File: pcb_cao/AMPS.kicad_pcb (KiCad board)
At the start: 2 copper layers, 80 x 36.2 mm, 21 parts, among them J1 Conn_01x02, J10 Conn_01x02, J11 Conn_01x02, J12 Conn_01x16, J2 Conn_01x02, J3 Conn_01x02, J4 Conn_01x02, J5 Conn_01x03, J6 Conn_01x03, J7 Conn_01x03, J8 Conn_01x03, U1 ARDUINO_MICRO_SHIELD

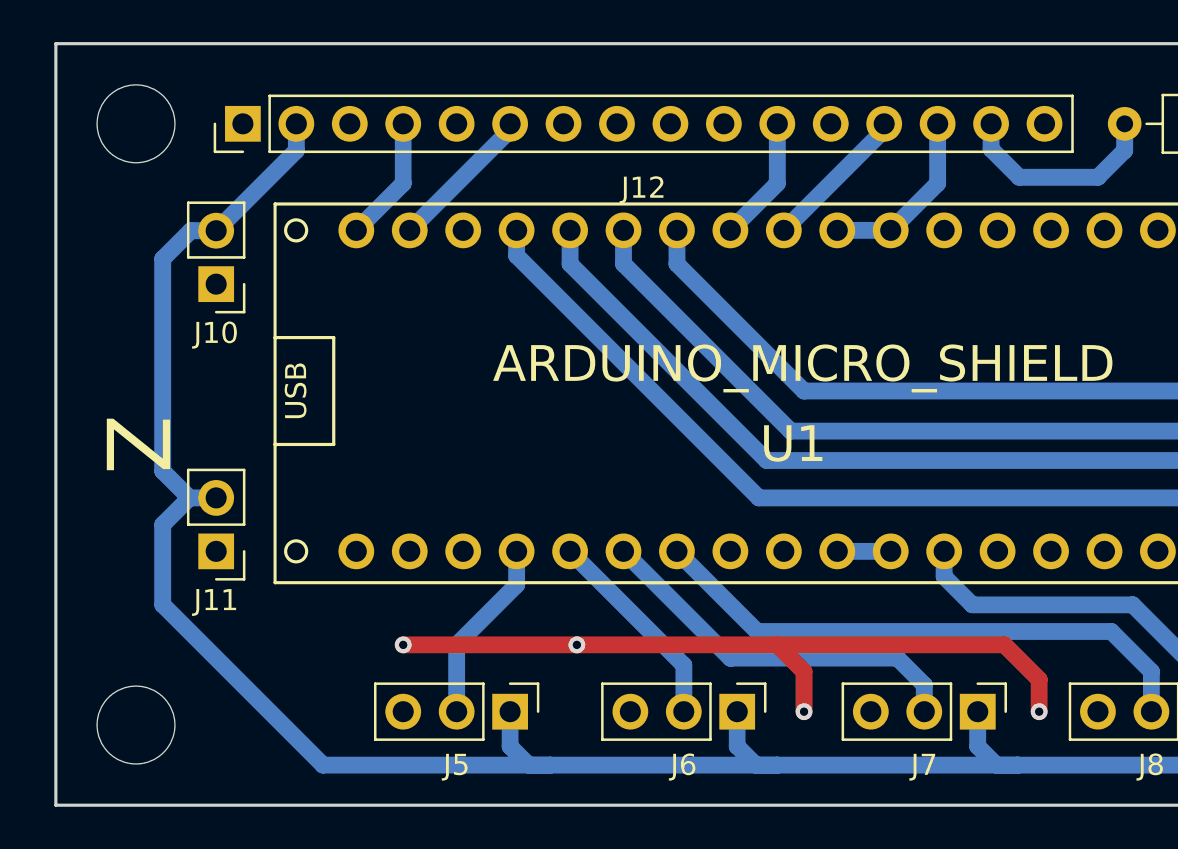
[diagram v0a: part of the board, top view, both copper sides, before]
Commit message: Fix routing problems
 - Duplicate pins tag on the LCD connexion
 - Fix Footprints references
 - Increase vias diameter
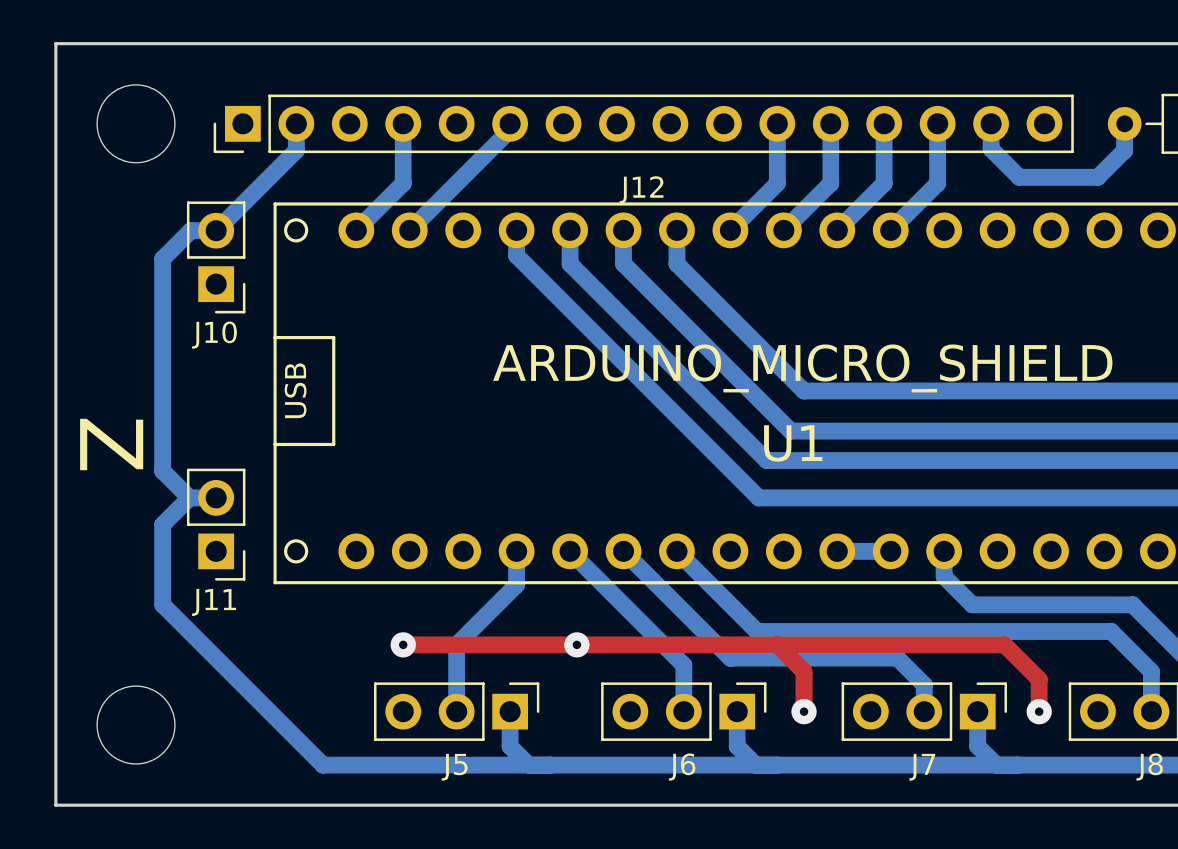
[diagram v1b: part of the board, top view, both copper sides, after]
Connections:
- U1 pad 3: D7 -> D6
- U1 pad 4: D6 -> D5
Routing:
- net D5: track 0.00 -> 5.99 mm
- net D7: track 8.53 -> 5.99 mm
- net D6: track 7.04 -> 6.28 mm

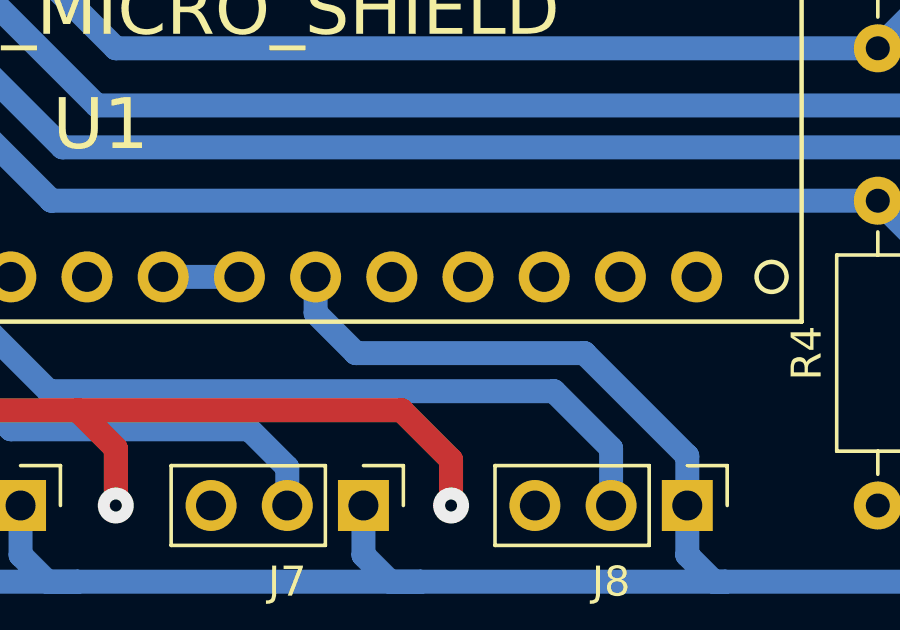
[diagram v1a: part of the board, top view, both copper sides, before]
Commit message: Power the arduino micro by pin 'Vin' not pin '5V'
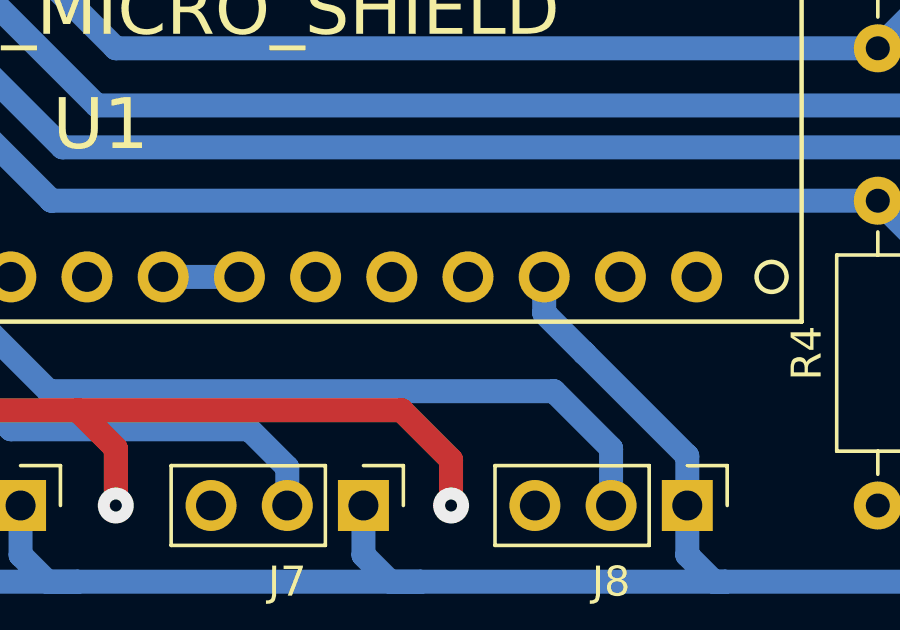
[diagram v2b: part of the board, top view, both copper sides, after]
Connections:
- U1 pad 5V: +5V -> Net-(U1-Pad5V)
- U1 pad VI: Net-(U1-PadVI) -> +5V
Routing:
- net +5V: track 179.9 -> 172.0 mm

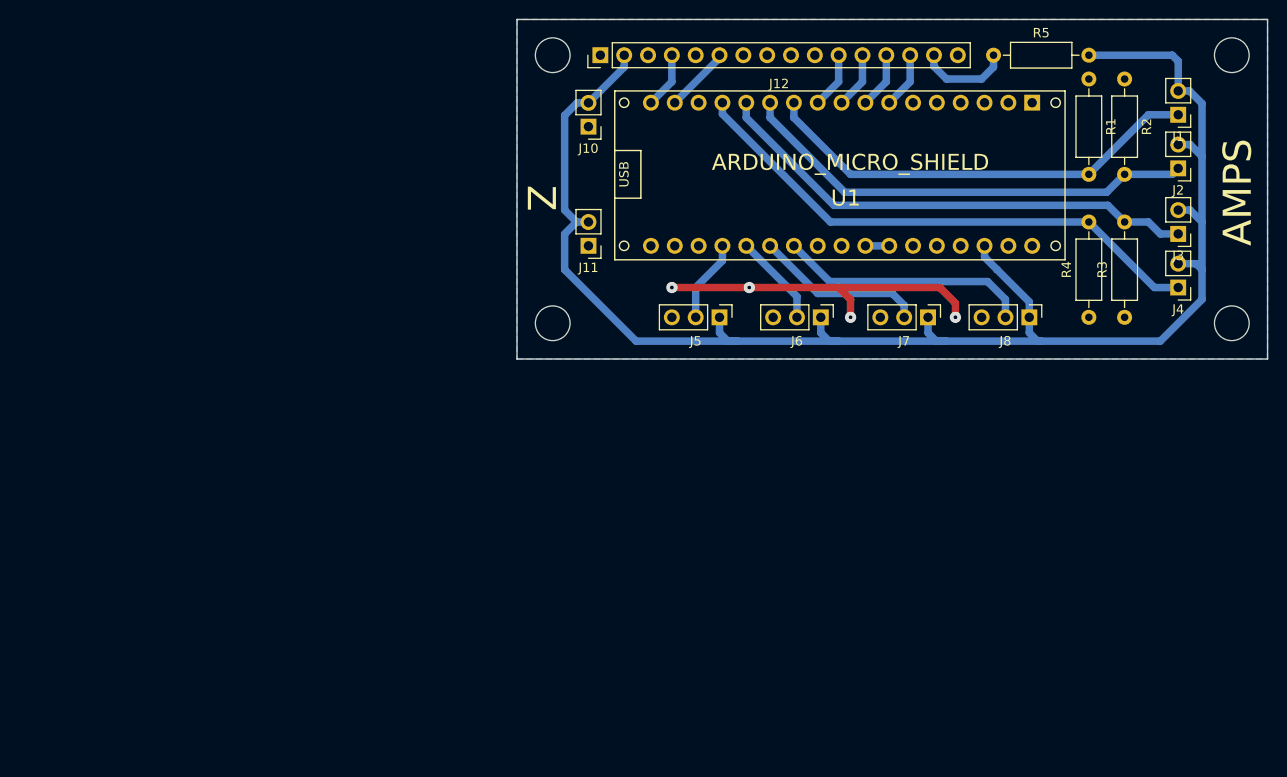
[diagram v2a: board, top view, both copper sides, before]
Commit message: Redesign of the PCB
Use a I2C LCD screen
Use only 2 buttons
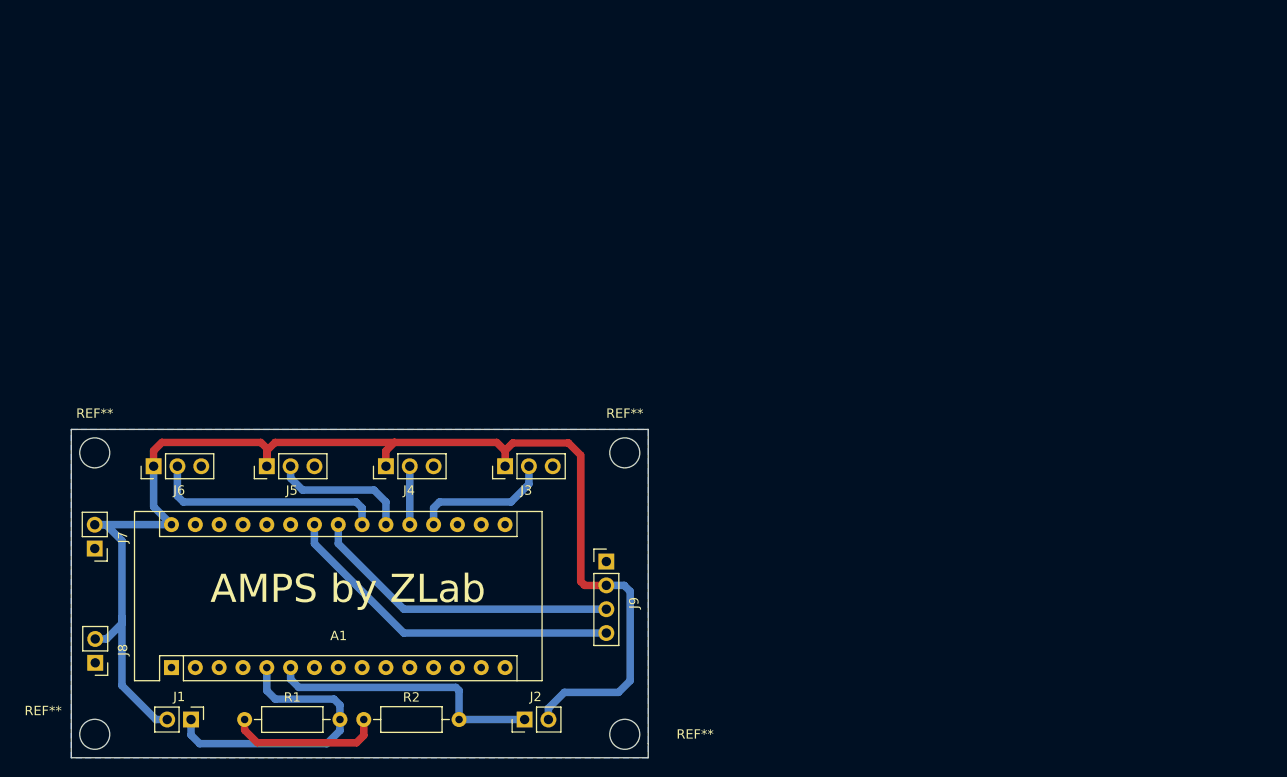
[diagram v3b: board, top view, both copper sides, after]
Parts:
- removed ? (x4): MountingHole_3.7mm, MountingHole:MountingHole_3.7mm
- removed J10, J11: Conn_01x02, Connector_PinHeader_2.54mm:PinHeader_1x02_P2.54mm_Vertical
- removed J12: Conn_01x16, Connector_PinHeader_2.54mm:PinHeader_1x16_P2.54mm_Vertical
- removed R3, R4: 10k, Resistor_THT:R_Axial_DIN0207_L6.3mm_D2.5mm_P10.16mm_Horizontal
- removed R5: 220, Resistor_THT:R_Axial_DIN0207_L6.3mm_D2.5mm_P10.16mm_Horizontal
- removed U1: ARDUINO_MICRO_SHIELD, Module:ARDUINO_MICRO_SHIELD
- added A1: Arduino_Nano_v3.x, Module:Arduino_Nano, F.Cu at (106.7, 119.9)
- added J9: Conn_01x04, Connector_PinHeader_2.54mm:PinHeader_1x04_P2.54mm_Vertical, F.Cu at (153.0, 108.6)
- added REF**: MountingHole_3.2mm_M3, MountingHole:MountingHole_3.2mm_M3, F.Cu at (155.0, 127.0)
- added REF**: MountingHole_3.2mm_M3, MountingHole:MountingHole_3.2mm_M3, F.Cu at (98.5, 127.0)
- added REF**: MountingHole_3.2mm_M3, MountingHole:MountingHole_3.2mm_M3, F.Cu at (98.5, 97.0)
- added REF**: MountingHole_3.2mm_M3, MountingHole:MountingHole_3.2mm_M3, F.Cu at (155.0, 97.0)
- J3, J4: value Conn_01x02 -> Conn_01x03; footprint Connector_PinHeader_2.54mm:PinHeader_1x02_P2.54mm_Vertical -> Connector_PinHeader_2.54mm:PinHeader_1x03_P2.54mm_Vertical
- J7, J8: value Conn_01x03 -> Conn_01x02; footprint Connector_PinHeader_2.54mm:PinHeader_1x03_P2.54mm_Vertical -> Connector_PinHeader_2.54mm:PinHeader_1x02_P2.54mm_Vertical
- moved J1 123.4 mm to (108.8, 125.4), turned to 270 degrees
- moved R1 113.0 mm to (114.5, 125.4), turned to 0 degrees
- moved J8 106.2 mm to (98.6, 119.4), turned to 180 degrees
- moved R2 106.0 mm to (127.2, 125.4), turned to 0 degrees
- moved J7 92.2 mm to (98.5, 107.2), turned to 180 degrees
- moved J2 91.1 mm to (144.3, 125.4), turned to 90 degrees
- moved J4 86.6 mm to (129.5, 98.4), turned to 90 degrees
- moved J3 75.9 mm to (142.2, 98.4), turned to 90 degrees
- moved J6 72.9 mm to (104.8, 98.4), turned to 90 degrees
- moved J5 50.8 mm to (116.8, 98.4), turned to 90 degrees
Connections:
- J3 pad 1: B3 -> +5V
- J3 pad 2: +5V -> I1_3.3V
- J4 pad 1: B4 -> +5V
- J4 pad 2: +5V -> I2_5V_USB
- J5 pad 2: I1_3.3V -> I3_5V
- J6 pad 2: I2_5V_USB -> I4_12V
- J7 pad 1: +5V -> GND
- J7 pad 2: I3_5V -> +5V
- J8 pad 1: +5V -> GND
- J8 pad 2: I4_12V -> +5V
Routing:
- net B4: track 57.4 -> 0.00 mm
- net B3: track 52.8 -> 0.00 mm
- net SDL: track 0.00 -> 37.1 mm
- net SDA: track 0.00 -> 33.5 mm
- net +5V: track 172.0 -> 142.2 mm
- net GND: track 36.1 -> 16.4 mm, vias 4 -> 0
- net B2: track 49.4 -> 29.9 mm
- net B1: track 47.7 -> 32.1 mm
- net Net-(J12-Pad15): track 9.90 -> 0.00 mm
- net E: track 7.04 -> 0.00 mm
- net D6: track 6.28 -> 0.00 mm
- net I1_3.3V: track 8.80 -> 14.9 mm
- net RS: track 5.99 -> 0.00 mm
- net D4: track 5.99 -> 0.00 mm
- net D7: track 5.99 -> 0.00 mm
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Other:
- board size 80 x 36.2 mm -> 61.5 x 35 mm
- net class Default: trace_width 0.25 -> 0.8; via_dia 0.8 -> 1; via_drill 0.4 -> 0.8
- rule pad_to_mask_clearance: 0.051 -> 0
- board text added: "AMPS by ZLab"
- board text removed: "AMPS"
- board text removed: "Z"
